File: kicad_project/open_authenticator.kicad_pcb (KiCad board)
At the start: 2 copper layers, 82 x 42 mm, 67 parts, among them IC1 TPS22919DCKR, J1 Conn_01x02_Female, J2 TYPE-C-31-M-17, J3 Conn_01x02_Female, P1 SSD1306_ribbon, Q1 DMP2305U-7, SW1 UP, SW2 DOWN, SW3 BOOT/SELECT, SW4 RESET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

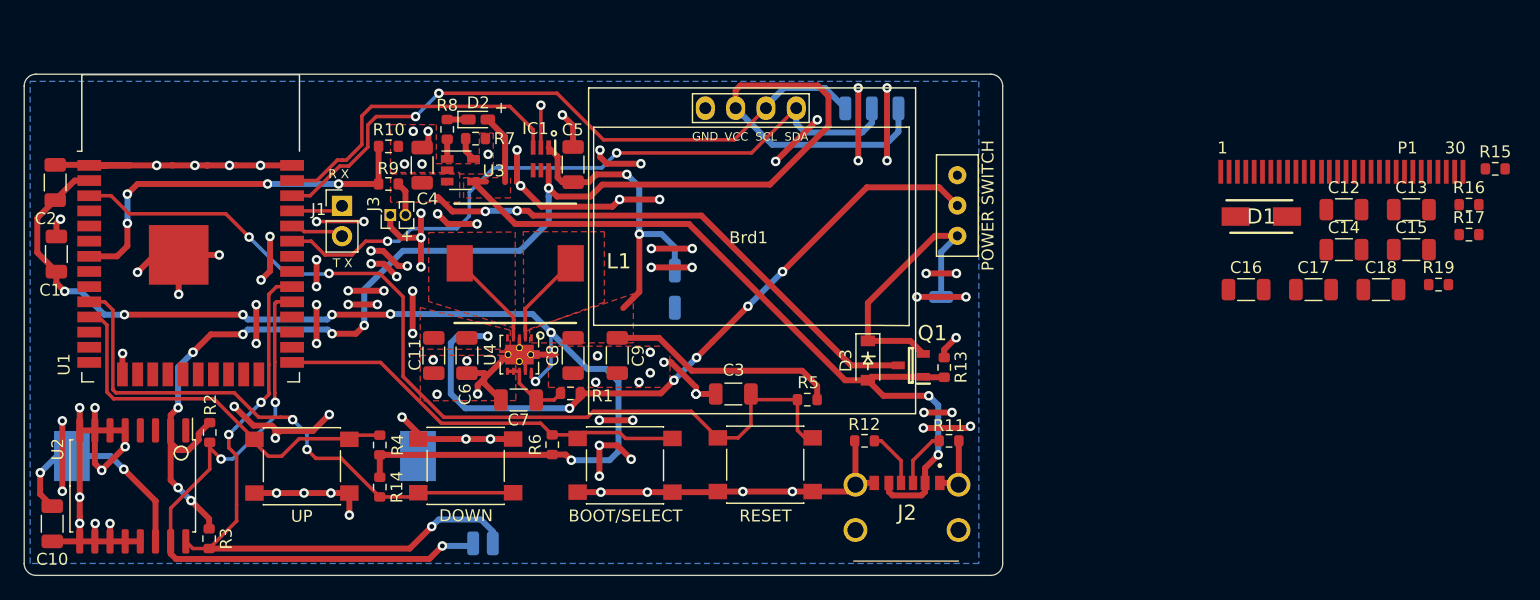
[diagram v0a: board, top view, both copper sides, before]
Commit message: Added 3d model for oled, and rerouted to reduce jumpovers and optimize current path
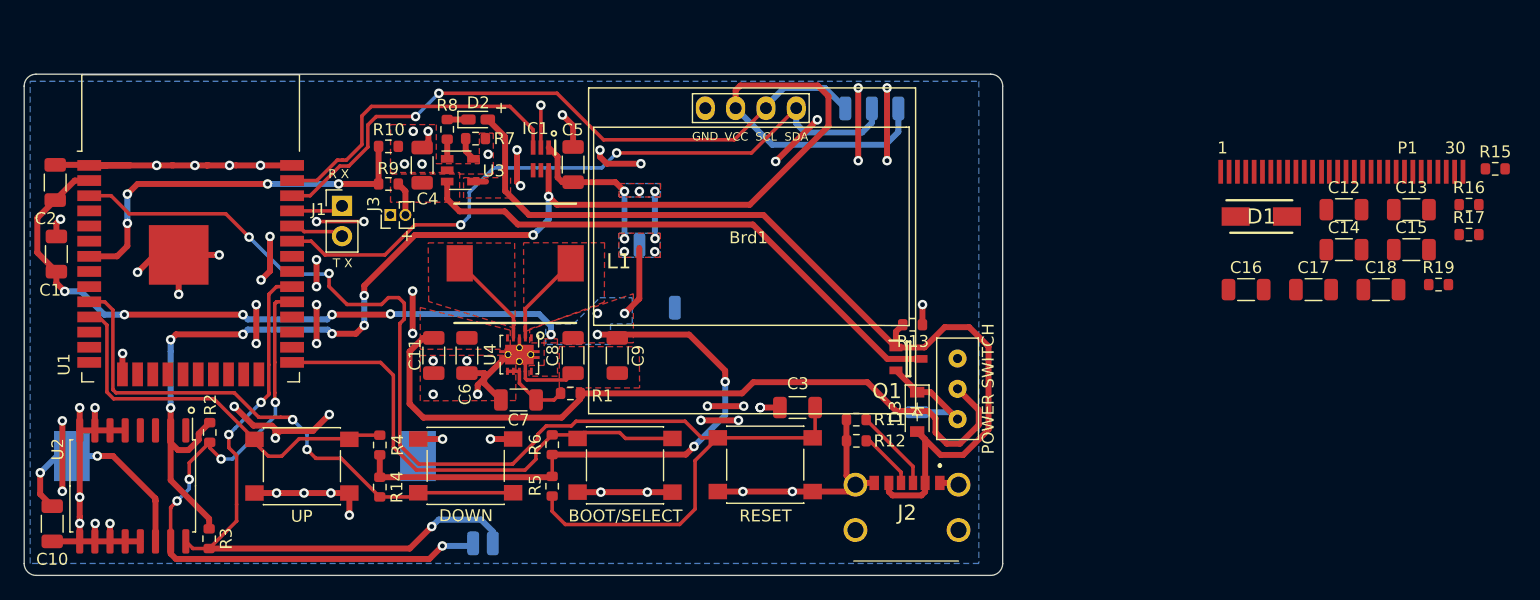
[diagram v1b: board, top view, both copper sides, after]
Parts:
- moved R5 22.6 mm to (134.2, 114.5), turned to 270 degrees
- moved SW5 15.4 mm to (168.2, 106.4)
- moved TP5 9.87 mm to (164.8, 108.3)
- moved R11 7.97 mm to (159.7, 108.9), turned to 0 degrees
- moved D3 5.96 mm to (164.8, 108.3)
- moved C3 5.50 mm to (154.8, 107.9)
- moved R13 4.45 mm to (164.4, 101.0), turned to 0 degrees
- moved TP1 3.66 mm to (141.6, 94.3)
- moved R12 0.69 mm to (159.7, 110.7)
- moved Q1 0.57 mm to (164.1, 103.9), turned to 0 degrees
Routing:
- net GND: track 285.5 -> 205.5 mm, vias 108 -> 71
- net /EN: track 79.5 -> 105.2 mm
- net +3V3: track 142.9 -> 128.6 mm, vias 10 -> 18
- net /V_INPUT: track 23.8 -> 10.5 mm
- net VBUS: track 71.9 -> 81.2 mm, vias 2 -> 0
- net /BOOT: track 34.9 -> 41.3 mm
- net Net-(C11-Pad1): track 59.1 -> 63.8 mm, vias 6 -> 0
- net +BATT: track 47.7 -> 49.9 mm, vias 2 -> 0
- net Net-(J2-PadB5): track 4.76 -> 6.93 mm
- net /LOAD_SWITCH_VCC: track 119.4 -> 121.4 mm
- net /IO5_SDA: vias 3 -> 5
- added copper zone on B.Cu, net +3V3

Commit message: Optimized routing further, used copper fill zones to change plane for routes with power
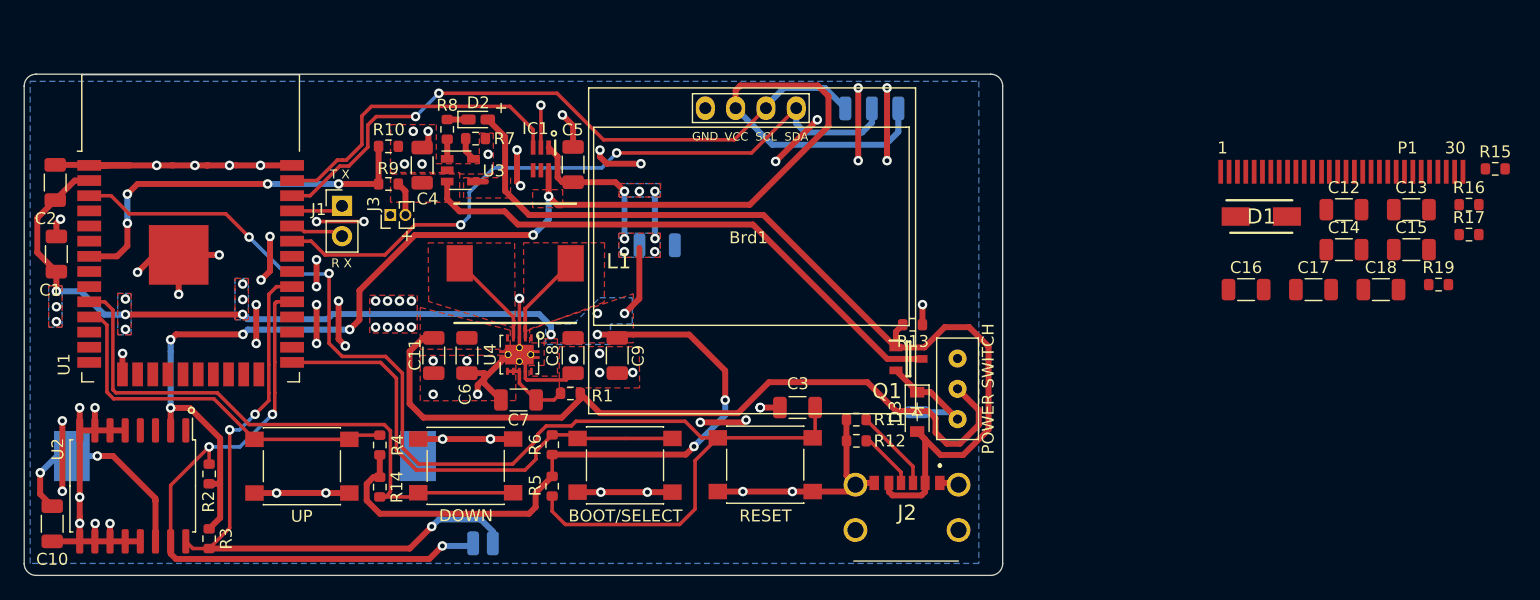
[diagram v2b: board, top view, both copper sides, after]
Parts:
- moved TP8 5.23 mm to (144.5, 94.3)
- moved R2 3.48 mm to (105.5, 113.5), turned to 90 degrees
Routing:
- net +3V3: track 128.6 -> 135.3 mm, vias 18 -> 22
- net GND: track 205.5 -> 199.0 mm, vias 71 -> 77
- net /IO25: track 47.1 -> 51.1 mm, vias 2 -> 0
- net /LOAD_SWITCH_VCC: track 121.4 -> 119.3 mm, vias 8 -> 6
- net /EN: track 105.2 -> 103.6 mm
- net /IO5_SDA: track 56.6 -> 55.1 mm, vias 5 -> 3
- net Net-(C11-Pad1): track 63.8 -> 65.2 mm
- net /IO26: track 33.4 -> 32.4 mm
- added copper zone on F.Cu, net /LOAD_SWITCH_VCC

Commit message: Fixed silkscreen issues
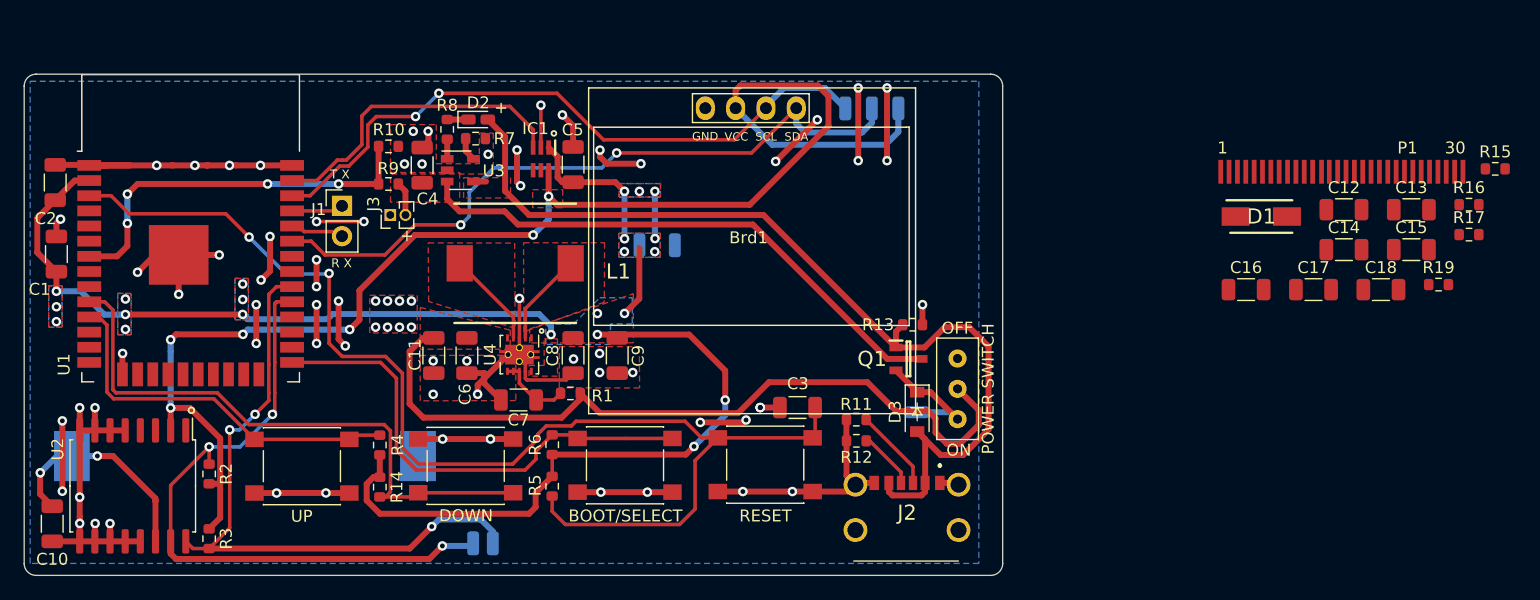
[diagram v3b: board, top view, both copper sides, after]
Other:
- board text added: "OFF"
- board text added: "ON"
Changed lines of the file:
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@@
   (general
     (thickness 1.6)
-    (drawings 25)
+    (drawings 27)
     (tracks 612)
     (zones 0)
@@
     (tags resistor)
     (attr smd)
-    (fp_text reference R2 (at -2.325 -0.05 90) (layer F.SilkS)
+    (fp_text reference R2 (at 0.00264 1.42892 90) (layer F.SilkS)
       (effects (font (size 1 1) (thickness 0.15)))
     )
@@
     (tags capacitor)
     (attr smd)
-    (fp_text reference C1 (at -3.0198 -0.5234 180) (layer F.SilkS)
+    (fp_text reference C1 (at -2.95122 -1.40732 180) (layer F.SilkS)
       (effects (font (size 1 1) (thickness 0.15)))
     )
@@
     (tags Inductor)
     (attr smd)
-    (fp_text reference L1 (at 8.677 -0.1682) (layer F.SilkS)
+    (fp_text reference L1 (at 8.64144 0.68524) (layer F.SilkS)
       (effects (font (size 1.27 1.27) (thickness 0.254)))
     )
@@
     (tags "MOSFET (P-Channel)")
     (attr smd)
-    (fp_text reference Q1 (at -1.8 2.7) (layer F.SilkS)
+    (fp_text reference Q1 (at -3.048 0) (layer F.SilkS)
       (effects (font (size 1.27 1.27) (thickness 0.254)))
     )
@@
     (tags resistor)
     (attr smd)
-    (fp_text reference R11 (at 2.79604 0.00254) (layer F.SilkS)
+    (fp_text reference R11 (at 0 -1.29032) (layer F.SilkS)
       (effects (font (size 1 1) (thickness 0.15)))
     )
@@
     (tags resistor)
     (attr smd)
-    (fp_text reference R12 (at 2.7954 0.0063) (layer F.SilkS)
+    (fp_text reference R12 (at 0.0014 1.37536) (layer F.SilkS)
       (effects (font (size 1 1) (thickness 0.15)))
     )
@@
     (tags resistor)
     (attr smd)
-    (fp_text reference R13 (at 0.025 1.4 180) (layer F.SilkS)
+    (fp_text reference R13 (at -2.8951 0 180) (layer F.SilkS)
       (effects (font (size 1 1) (thickness 0.15)))
     )
@@
     )
   )
+  (gr_text ON (at 168.3258 111.506) (layer F.SilkS)
+    (effects (font (size 1 1) (thickness 0.1)))
+  )
+  (gr_text OFF (at 168.20134 101.27996) (layer F.SilkS)
+    (effects (font (size 1 1) (thickness 0.1)))
+  )
   (dimension 82 (width 0.15) (layer Dwgs.User)
     (gr_text "82.000 mm" (at 131 125.4044) (layer Dwgs.User)
@@
   )
   (gr_circle (center 134.3914 84.963) (end 134.3914 84.763) (layer F.SilkS) (width 0.15))
-  (gr_circle (center 133.25 101.9) (end 133.532843 101.9) (layer F.SilkS) (width 0.15))
+  (gr_circle (center 133.3627 101.51618) (end 133.52874 101.49304) (layer F.SilkS) (width 0.15))
   (gr_circle (center 104.01046 108.16336) (end 104.21814 108.04382) (layer F.SilkS) (width 0.15))
   (gr_text "v1.3 Vedant Paranjape" (at 101.65 84.9) (layer B.SilkS)

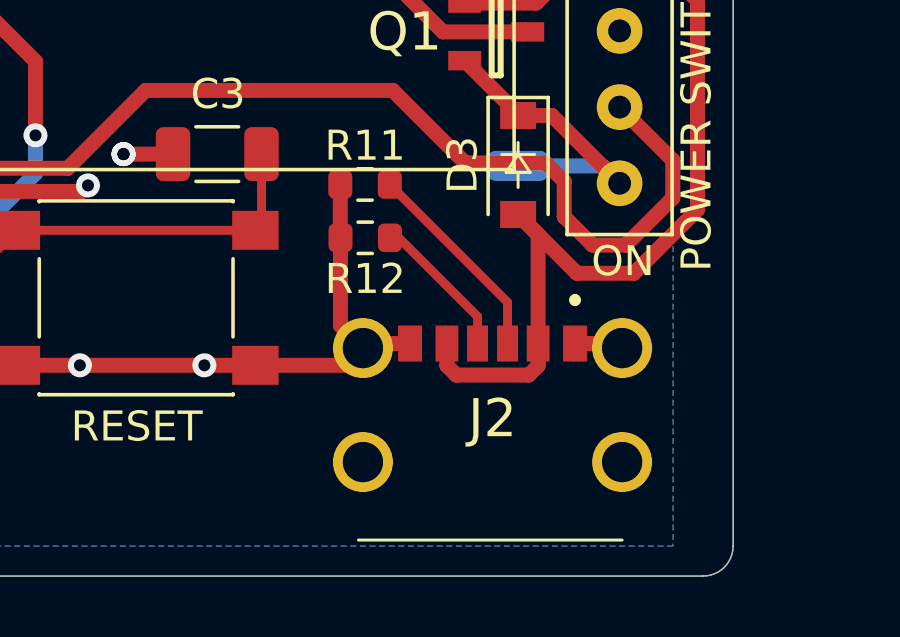
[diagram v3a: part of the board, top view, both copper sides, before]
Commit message: Assigned OLED 3d model to it's footprint and moved USB-C port towards the edge
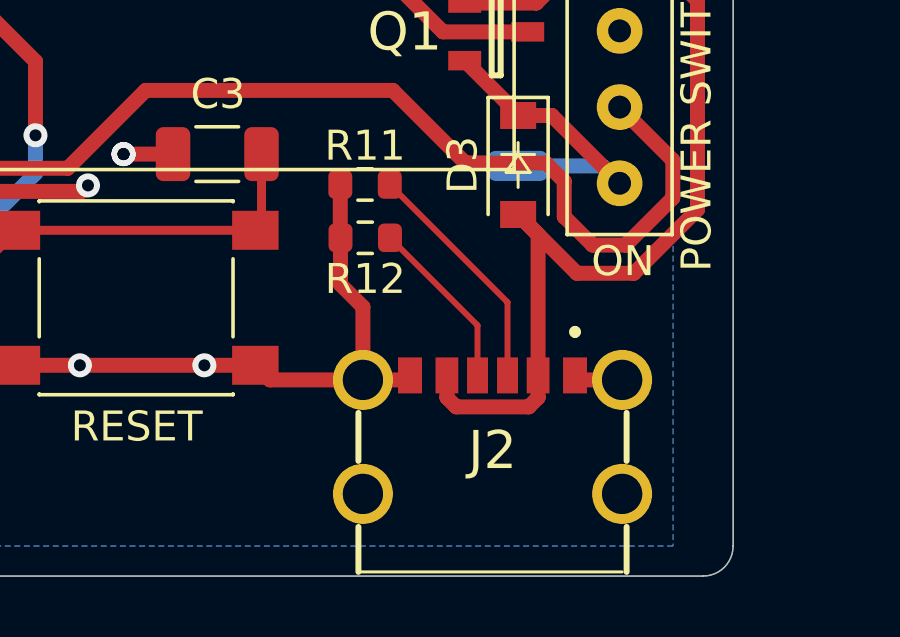
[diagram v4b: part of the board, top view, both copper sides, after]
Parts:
- moved J2 1.06 mm to (164.0, 117.8)
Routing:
- net VBUS: track 81.2 -> 82.2 mm
- net Net-(J2-PadB5): track 6.93 -> 7.99 mm
- net Net-(J2-PadA5): track 4.91 -> 5.80 mm
- net GND: track 199.0 -> 199.6 mm

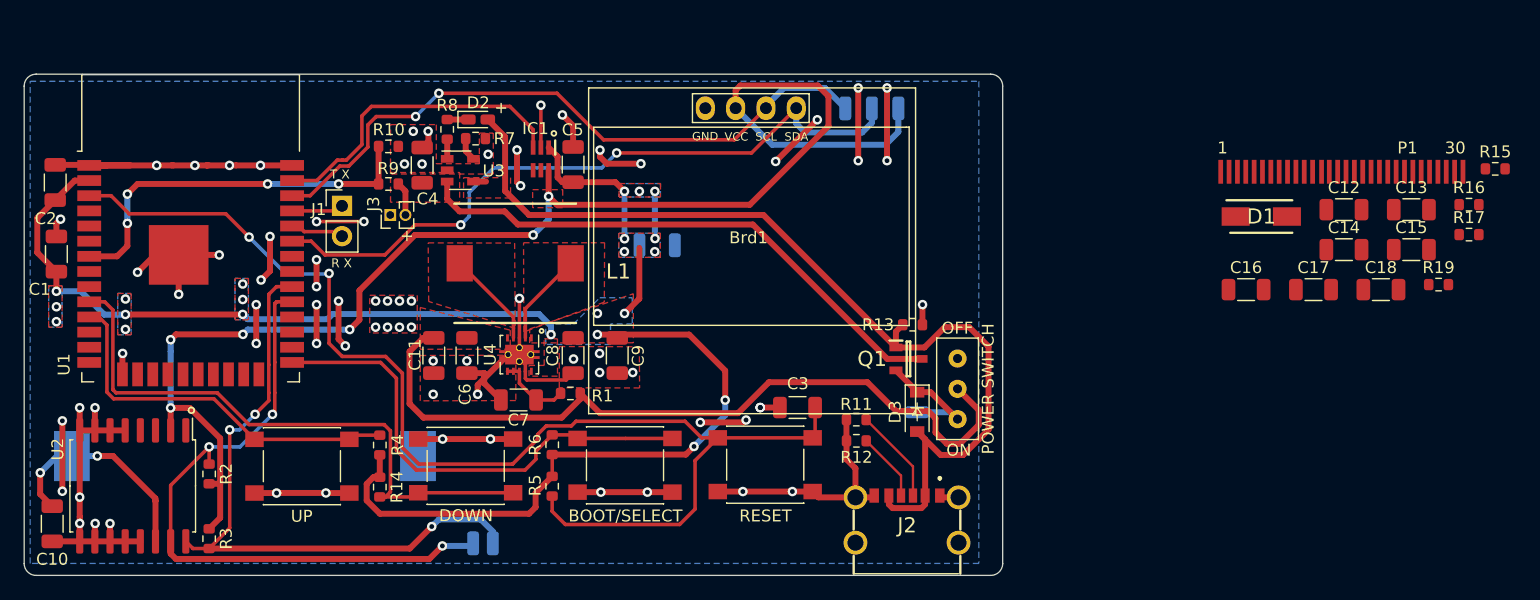
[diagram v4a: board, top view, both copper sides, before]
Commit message: [WIP] Started routing components used for OLED sub circuit
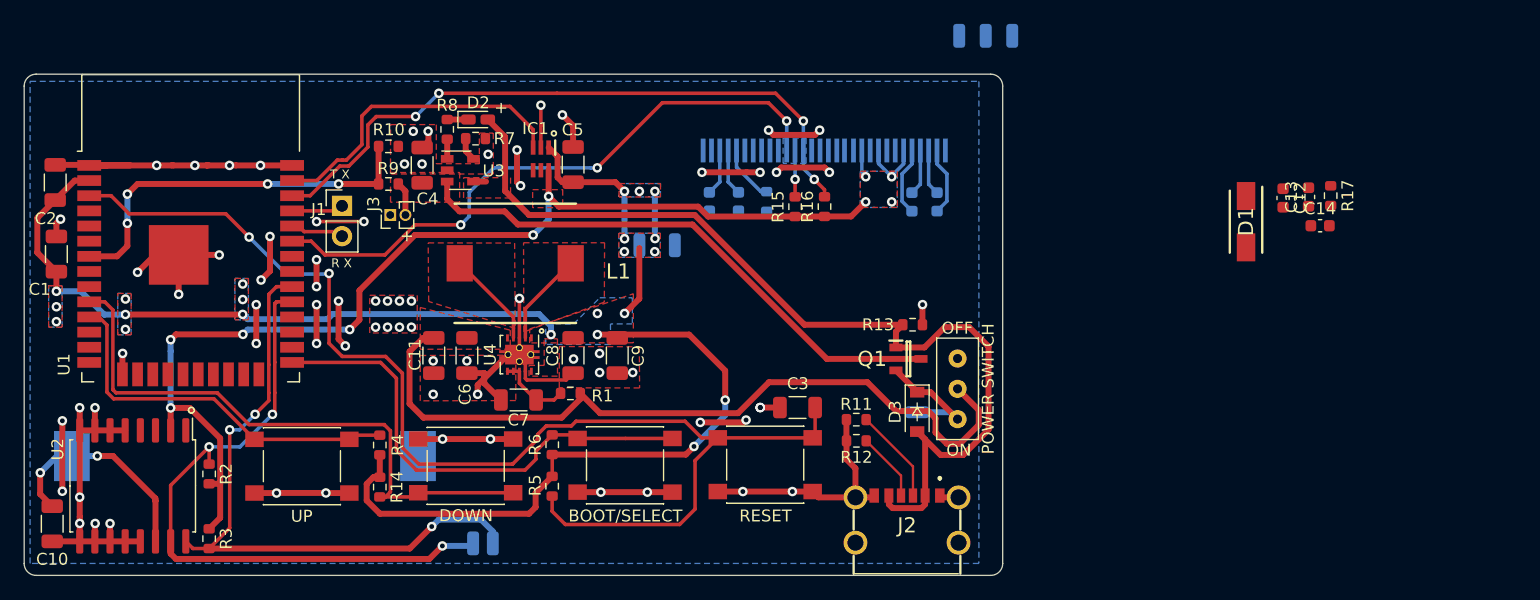
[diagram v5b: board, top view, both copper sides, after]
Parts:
- removed Brd1: SSD1306, SSD1306:128x64OLED
- removed REF**: KiCad-Logo2_5mm_SilkScreen, Symbol:KiCad-Logo2_5mm_SilkScreen
- removed REF**: OSHW-Logo2_9.8x8mm_SilkScreen, Symbol:OSHW-Logo2_9.8x8mm_SilkScreen
- C12: value 10uF 50V -> 10uF 16V; footprint Capacitor_SMD:C_1206_3216Metric -> Capacitor_SMD:C_0603_1608Metric
- C13, C14: value 0.1uF 50V -> 0.1uF 16V; footprint Capacitor_SMD:C_1206_3216Metric -> Capacitor_SMD:C_0603_1608Metric
- C15: value 4.7uF 50V -> 4.7uF 16V; footprint Capacitor_SMD:C_1206_3216Metric -> Capacitor_SMD:C_0603_1608Metric; moved to B.Cu
- C16: value 2.2uF 50V -> 2.2uF 16V; footprint Capacitor_SMD:C_1206_3216Metric -> Capacitor_SMD:C_0603_1608Metric; moved to B.Cu
- C17, C18: footprint Capacitor_SMD:C_1206_3216Metric -> Capacitor_SMD:C_0603_1608Metric; moved to B.Cu
- P1, R19: moved to B.Cu
- moved R15 58.8 mm to (154.6, 91.1), turned to 90 degrees
- moved R19 56.7 mm to (152.2, 90.7), turned to 90 degrees
- moved C15 56.5 mm to (149.9, 90.7), turned to 90 degrees
- moved R16 54.0 mm to (157.1, 91.1), turned to 90 degrees
- moved C16 45.6 mm to (147.4, 90.7), turned to 90 degrees
- moved P1 43.4 mm to (157.0, 86.4), turned to 180 degrees
- moved C18 40.0 mm to (164.4, 90.7), turned to 90 degrees
- moved C17 32.4 mm to (166.5, 90.7), turned to 90 degrees
- moved R17 12.0 mm to (199.5, 90.2), turned to 270 degrees
- moved TP4 11.3 mm to (172.8, 76.8)
- moved TP6 11.3 mm to (170.6, 76.8)
- moved TP7 11.3 mm to (168.4, 76.8)
- moved C13 8.68 mm to (197.6, 90.3), turned to 90 degrees
- moved C12 5.19 mm to (195.5, 90.4), turned to 270 degrees
- moved C14 2.83 mm to (198.6, 92.7)
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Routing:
- net /LOAD_SWITCH_VCC: track 119.3 -> 98.6 mm, vias 6 -> 10
- net GND: track 199.6 -> 192.3 mm, vias 77 -> 74
- net Net-(C18-Pad1): track 0.00 -> 5.77 mm
- net Net-(C17-Pad1): track 0.00 -> 5.76 mm
- net Net-(P1-Pad26): track 0.00 -> 4.77 mm
- net /IO21_SDA: track 59.3 -> 55.4 mm, vias 2 -> 4
- net Net-(C16-Pad2): track 0.00 -> 3.87 mm
- net Net-(C15-Pad2): track 0.00 -> 3.86 mm
- net Net-(C18-Pad2): track 0.00 -> 3.83 mm
- net Net-(C17-Pad2): track 0.00 -> 3.82 mm
- net /IO22_SCL: track 55.8 -> 55.5 mm, vias 2 -> 4
- added copper zone on B.Cu, net /IO21_SDA
- added copper zone on B.Cu, net /LOAD_SWITCH_VCC
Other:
- board text removed: "GND"
- board text removed: "SCL"
- board text removed: "SDA"
- board text removed: "VCC"
